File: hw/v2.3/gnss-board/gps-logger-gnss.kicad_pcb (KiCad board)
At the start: 4 copper layers, 41.4 x 45 mm, 17 parts, among them J1 Conn_01x06_MountingPin, U1 MAX-M8C, U2 BGU7007

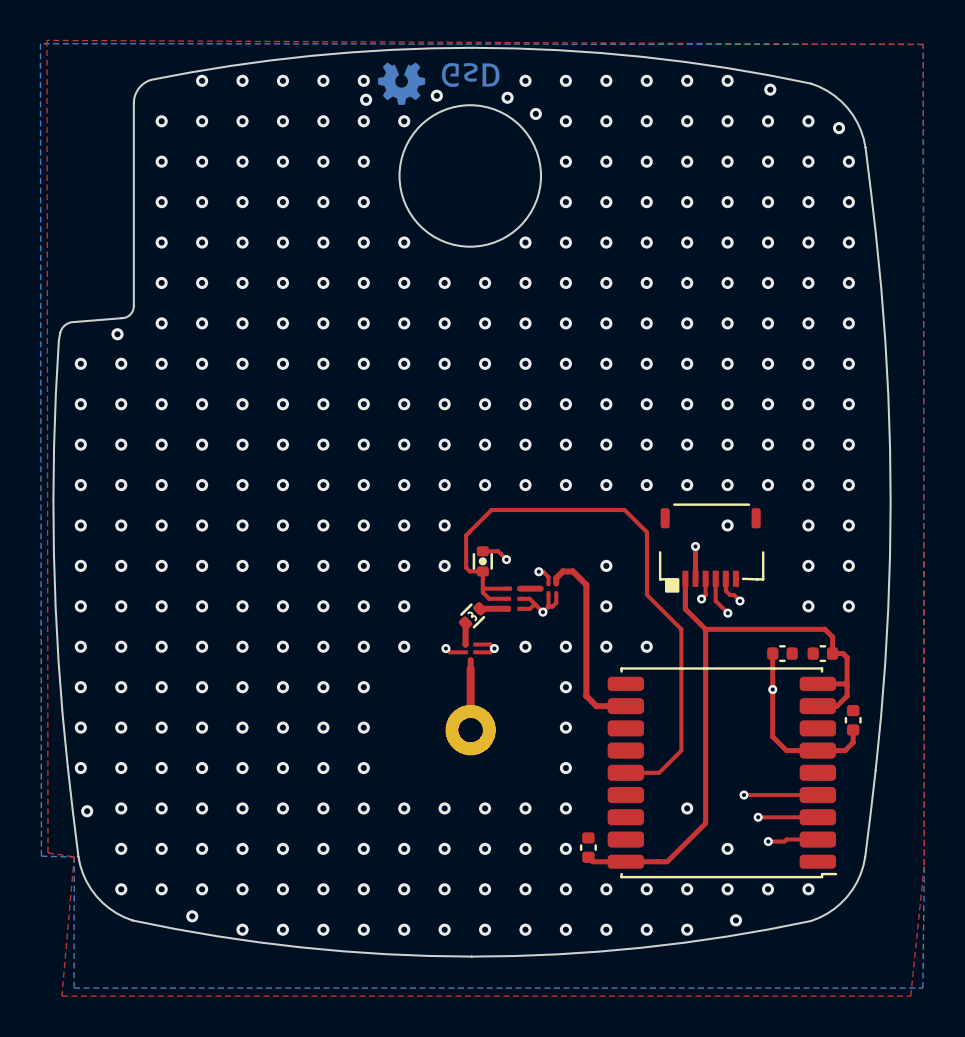
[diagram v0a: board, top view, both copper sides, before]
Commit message: Update r2.3
- Add make panel KiKit script
- Add production gerbers
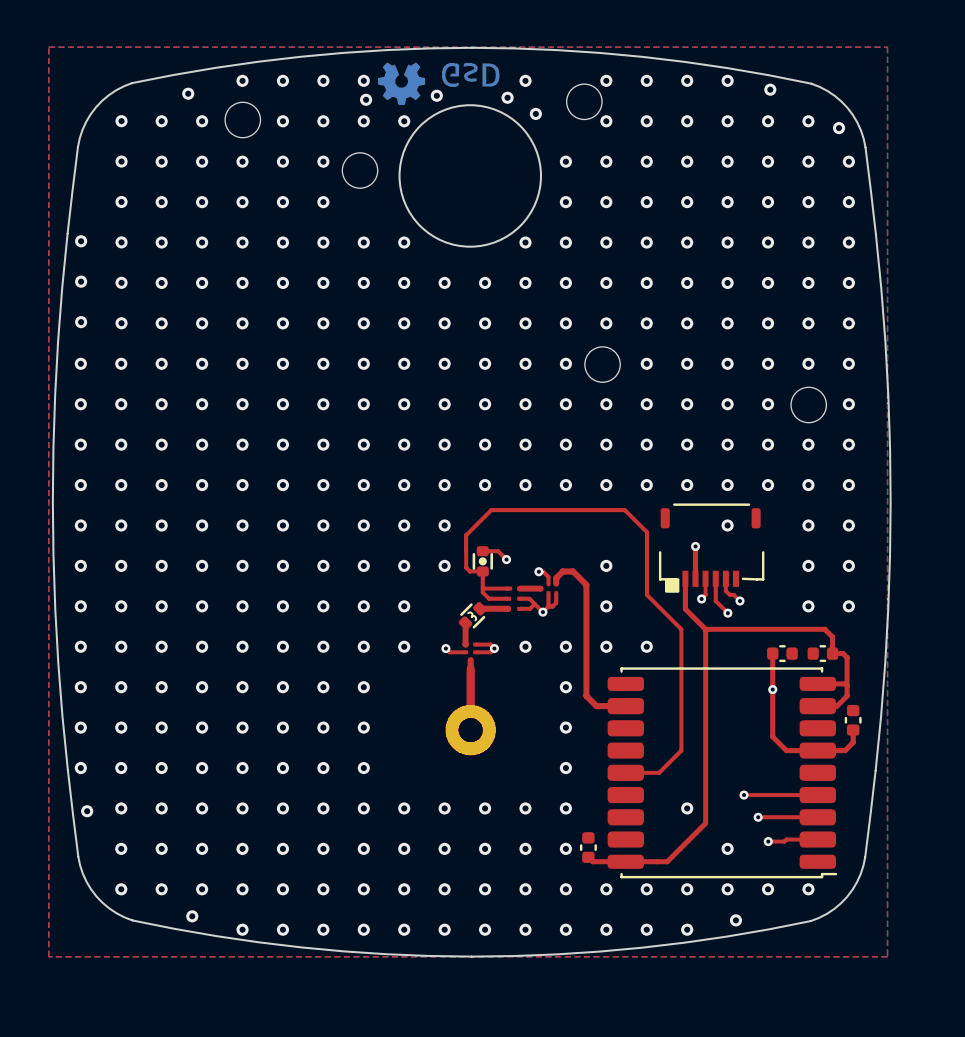
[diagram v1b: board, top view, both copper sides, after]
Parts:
- added REF**: M1.6_Mounting Hole, gps-logger:M1.6_Mounting Hole, F.Cu at (114.6, 85.0)
- added REF**: M1.6_Mounting Hole, gps-logger:M1.6_Mounting Hole, F.Cu at (102.6, 75.4)
- added REF**: M1.6_Mounting Hole, gps-logger:M1.6_Mounting Hole, F.Cu at (96.8, 72.9)
- added REF**: M1.6_Mounting Hole, gps-logger:M1.6_Mounting Hole, F.Cu at (113.7, 72.0)
- added REF**: M1.6_Mounting Hole, gps-logger:M1.6_Mounting Hole, F.Cu at (124.8, 87.0)
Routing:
- net GND: vias 334 -> 335
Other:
- board size 41.4 x 45 mm -> 41.5 x 45 mm

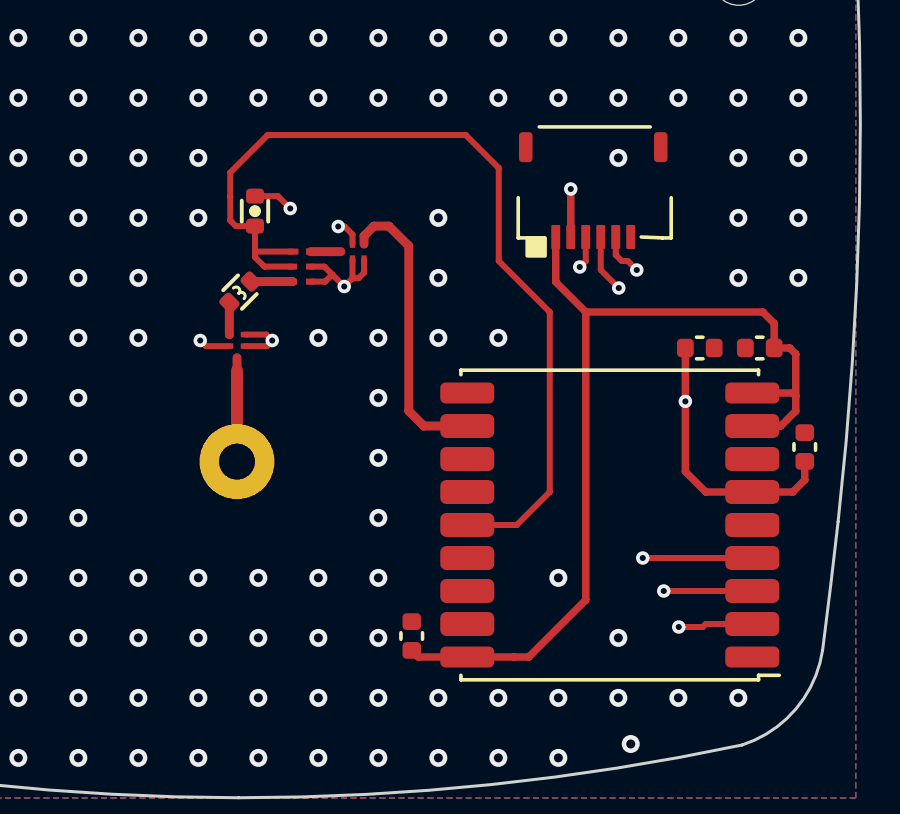
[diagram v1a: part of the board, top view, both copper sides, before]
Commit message: Update PCBs to remove small vias
- Regenerate 1x panel
- Add gerbers
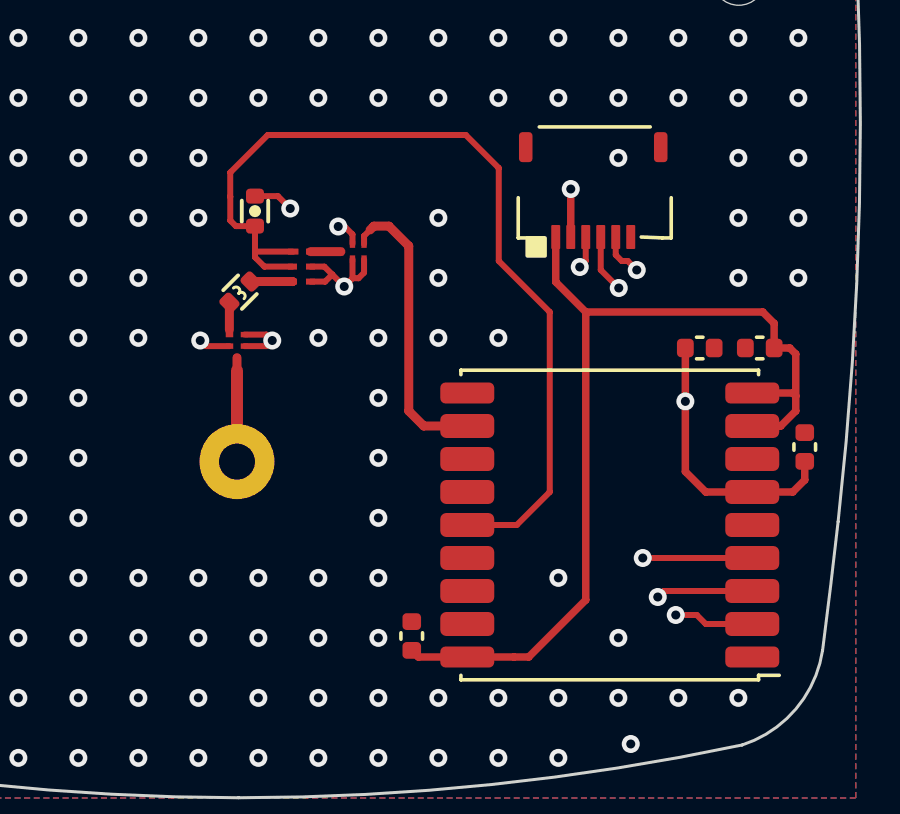
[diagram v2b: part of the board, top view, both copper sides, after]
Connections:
- FLT1 pad 2: (no net) -> GND
- FLT1 pad 4: (no net) -> GND
- FLT1 pad 5: (no net) -> GND
- FLT2 pad 1: Net-(FLT2-Pad1) -> Net-(ANT1-Pad1)
- FLT2 pad 2: (no net) -> GND
- FLT2 pad 4: (no net) -> GND
- FLT2 pad 5: (no net) -> GND
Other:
- rule pad_to_mask_clearance: 0.05 -> 0
